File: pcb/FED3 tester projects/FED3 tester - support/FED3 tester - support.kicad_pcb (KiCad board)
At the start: 2 copper layers, 108 x 82 mm, 27 parts, among them J2 6pin_hd

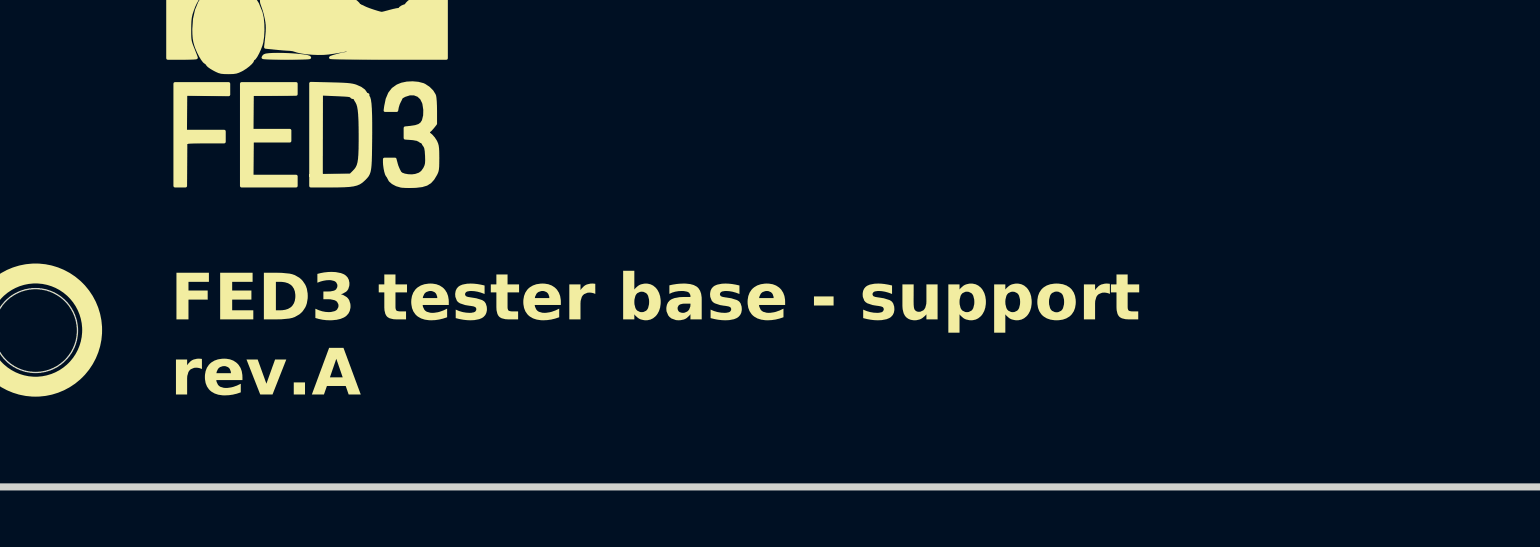
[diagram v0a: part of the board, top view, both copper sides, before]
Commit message: alteração no nome do projecto "FED3 tester - support"
. gerados novos Gerbers & Drill & .d356
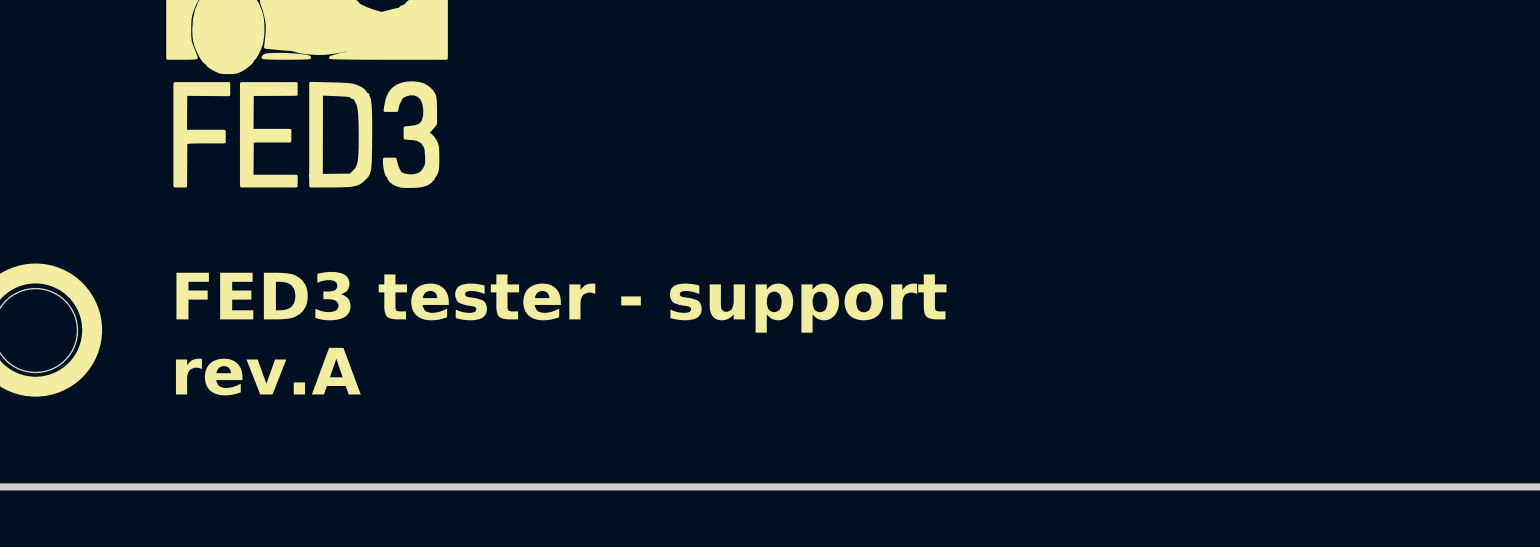
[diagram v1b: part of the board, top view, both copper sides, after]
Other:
- board text added: "FED3 tester - support rev.A"
- board text removed: "FED3 tester base - support rev.A"
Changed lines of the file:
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@@
 		(layer "F.Fab")
 	)
-	(gr_text "FED3 tester base - support\nrev.A"
+	(gr_text "FED3 tester - support\nrev.A"
 		(at 112.25 112.05 0)
 		(layer "F.SilkS")

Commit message: FED3 tester rev.B & FED3 tester support rev.B
-rev.B para 1ª revisão do Filipe
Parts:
- added ?: , , F.Cu at (55.8, 166.7)
- added ?: , , F.Cu at (142.8, 166.7)
- added ?: , , F.Cu at (101.0, 156.5)
- added ?: , , F.Cu at (141.6, 156.5)
- moved G*** 72.1 mm to (59.6, 141.8)
- moved ? 51.9 mm to (99.7, 74.3)
- moved ? 51.9 mm to (146.6, 44.3)
- moved ? 51.9 mm to (142.9, 93.3)
- moved TP13 51.9 mm to (88.6, 63.8)
- moved TP6 51.9 mm to (84.8, 78.9)
- moved ? 51.9 mm to (55.8, 114.4)
- moved ? 51.9 mm to (52.0, 44.3)
- moved ? 51.9 mm to (54.0, 82.9)
- moved TP10 51.9 mm to (47.0, 57.4)
- moved TP11 51.9 mm to (68.3, 65.6)
- moved TP12 51.9 mm to (83.6, 70.6)
- moved TP2 51.9 mm to (125.5, 85.9)
- moved TP3 51.9 mm to (67.5, 62.7)
- moved TP4 51.9 mm to (55.7, 69.5)
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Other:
- board size 108 x 82 mm -> 108 x 134.3 mm
- board text added: "FED3 tester - support rev.B"
- board text removed: "FED3 tester - support rev.A"
